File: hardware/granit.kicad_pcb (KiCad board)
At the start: 4 copper layers, 92 x 100 mm, 4 parts

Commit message: Draft component placement
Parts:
- added BT1: Battery_Cell, Battery:BatteryHolder_Keystone_3034_1x20mm, F.Cu at (32.0, 37.0)
- added C1: 10u, Capacitor_SMD:C_0805_2012Metric, F.Cu at (57.0, 104.5)
- added C10: 100u, Capacitor_Tantalum_SMD:CP_EIA-7343-31_Kemet-D, F.Cu at (55.0, 114.5)
- added C11: 100n, Capacitor_SMD:C_0805_2012Metric, F.Cu at (78.0, 115.5)
- added C12: 1n, Capacitor_SMD:C_0805_2012Metric, F.Cu at (65.0, 111.0)
- added C13: 10u, Capacitor_SMD:C_0805_2012Metric, F.Cu at (81.5, 111.0)
- added C14: 10u, Capacitor_SMD:C_0805_2012Metric, F.Cu at (87.5, 114.5)
- added C15: 10u, Capacitor_SMD:C_0805_2012Metric, F.Cu at (85.5, 114.5)
- added C16: 10u, Capacitor_SMD:C_0805_2012Metric, F.Cu at (83.5, 114.5)
- added C17: 10u, Capacitor_SMD:C_0805_2012Metric, F.Cu at (85.5, 111.0)
- added C18: 10u, Capacitor_SMD:C_0805_2012Metric, F.Cu at (83.5, 111.0)
- added C19: 100n, Capacitor_SMD:C_0805_2012Metric, F.Cu at (78.0, 107.5)
- added C2: 10u, Capacitor_SMD:C_0805_2012Metric, F.Cu at (54.0, 96.5)
- added C20: 1n, Capacitor_SMD:C_0805_2012Metric, F.Cu at (69.0, 110.0)
- added C21: 1.2n, Capacitor_SMD:C_0805_2012Metric, F.Cu at (70.0, 107.0)
- added C22: 100n, Capacitor_SMD:C_0805_2012Metric, F.Cu at (95.5, 80.0)
- added C23: 100n, Capacitor_SMD:C_0805_2012Metric, F.Cu at (39.0, 52.5)
- added C24: 100n, Capacitor_SMD:C_0805_2012Metric, F.Cu at (41.5, 52.5)
- added C25: 100n, Capacitor_SMD:C_0805_2012Metric, F.Cu at (36.5, 52.5)
- added C26: 15p, Capacitor_SMD:C_0805_2012Metric, F.Cu at (41.5, 73.0)
- added C27: 15p, Capacitor_SMD:C_0805_2012Metric, F.Cu at (39.5, 73.0)
- added C28: 100n, Capacitor_SMD:C_0805_2012Metric, F.Cu at (29.5, 68.0)
- added C29: 100n, Capacitor_SMD:C_0805_2012Metric, F.Cu at (32.0, 52.0)
- added C3: 10u, Capacitor_SMD:C_0805_2012Metric, F.Cu at (95.0, 109.5)
- added C30: 100n, Capacitor_SMD:C_0805_2012Metric, F.Cu at (37.5, 58.5)
- added C31: 100n, Capacitor_SMD:C_0805_2012Metric, F.Cu at (39.5, 58.5)
- added C32: 100n, Capacitor_SMD:C_0805_2012Metric, F.Cu at (35.5, 73.5)
- added C33: 100n, Capacitor_SMD:C_0805_2012Metric, F.Cu at (30.0, 62.0)
- added C34: 100n, Capacitor_SMD:C_0805_2012Metric, F.Cu at (103.5, 35.0)
- added C35: 100n, Capacitor_SMD:C_0805_2012Metric, F.Cu at (100.0, 30.0)
- added C36: 100n, Capacitor_SMD:C_0805_2012Metric, F.Cu at (100.0, 48.5)
- added C37: 100n, Capacitor_SMD:C_0805_2012Metric, F.Cu at (48.1, 34.6)
- added C38: 100n, Capacitor_SMD:C_0805_2012Metric, F.Cu at (109.0, 58.0)
- added C39: 100n, Capacitor_SMD:C_0805_2012Metric, F.Cu at (52.1, 34.3)
- added C4: 10u, Capacitor_SMD:C_0805_2012Metric, F.Cu at (94.5, 117.5)
- added C5: 10u, Capacitor_SMD:C_0805_2012Metric, F.Cu at (81.5, 114.5)
- added C6: 10u, Capacitor_SMD:C_0805_2012Metric, F.Cu at (63.0, 111.0)
- added C7: 10u, Capacitor_SMD:C_0805_2012Metric, F.Cu at (61.0, 111.0)
- added C8: 10u, Capacitor_SMD:C_0805_2012Metric, F.Cu at (63.0, 114.5)
- added C9: 10u, Capacitor_SMD:C_0805_2012Metric, F.Cu at (61.0, 114.5)
- added CM1: CM4, granit:Raspberry-Pi-4-Compute-Module, F.Cu at (85.5, 42.0)
- added D1: SK6812MINI-E, LED_SMD:LED_SK6812MINI-E_3.2x2.8mm_P1.5mm_ReverseMount, F.Cu at (109.0, 32.0)
- added D2: LED R, LED_SMD:LED_0805_2012Metric, F.Cu at (91.5, 35.5)
- added D3: LED G, LED_SMD:LED_0805_2012Metric, F.Cu at (91.5, 31.1)
- added F1: Fuse, Fuse:Fuse_2512_6332Metric, F.Cu at (99.5, 112.5)
- added IC1: ASM1061, granit:QFN50P700X700X90-49N-D, F.Cu at (35.5, 65.5)
- added J1: 12V Barrel, granit:BarrelJack_Wuerth_6941xx301002, F.Cu at (97.4, 102.8)
- added J2: 12V Screw Terminal, TerminalBlock_Phoenix:TerminalBlock_Phoenix_MKDS-1,5-2_1x02_P5.00mm_Horizontal, F.Cu at (107.1, 104.8)
- added J3: RJ45_RB1-125B8G1A, Connector_RJ:RJ45_UDE_RB1-125B8G1A, F.Cu at (93.8, 75.8)
- added J6: Conn_01x02, Connector_PinHeader_2.54mm:PinHeader_1x02_P2.54mm_Vertical, F.Cu at (78.3, 29.5)
- added J7: USB_C_Receptacle_USB2.0_14P, Connector_USB:USB_C_Receptacle_GCT_USB4105-xx-A_16P_TopMnt_Horizontal, F.Cu at (108.5, 51.5)
- added J8: Conn_01x03, Connector_PinHeader_2.54mm:PinHeader_1x03_P2.54mm_Vertical, F.Cu at (82.0, 29.5)
- added J9: SATA_22pin, Connector_SATA_SAS:SATA_Amphenol_10029364-001LF_Horizontal, F.Cu at (23.0, 79.5)
- added JP1: 12V_bridge, Jumper:SolderJumper-2_P1.3mm_Open_Pad1.0x1.5mm, F.Cu at (29.0, 105.5)
- added JP2: 5V_bridge, Jumper:SolderJumper-2_P1.3mm_Open_Pad1.0x1.5mm, F.Cu at (39.5, 116.5)
- added JP3: 3V3_bridge, Jumper:SolderJumper-2_P1.3mm_Open_Pad1.0x1.5mm, F.Cu at (47.0, 97.0)
- added JP4: USB_OTG, Jumper:SolderJumper-2_P1.3mm_Bridged_Pad1.0x1.5mm, F.Cu at (44.5, 83.5)
- added L1: SRN6045TA-3R3Y, Inductor_SMD:L_Bourns_SRN6045TA, F.Cu at (67.5, 116.1)
- added Q1: FDS4435BZ, granit:SO08-E3, F.Cu at (93.5, 113.6)
- added Q2: FDS4435BZ, granit:SO08-E3, F.Cu at (33.5, 106.0)
- added Q3: FDS4435BZ, granit:SO08-E3, F.Cu at (41.0, 112.0)
- added Q4: 2N7002, Package_TO_SOT_SMD:SOT-23, F.Cu at (71.5, 35.6)
- added R1: 10R, Resistor_SMD:R_0805_2012Metric, F.Cu at (74.5, 115.5)
- added R10: 12K, Resistor_SMD:R_0805_2012Metric, F.Cu at (34.0, 58.5)
- added R11: 750R, Resistor_SMD:R_0805_2012Metric, F.Cu at (27.5, 65.5)
- added R12: 100K, Resistor_SMD:R_0805_2012Metric, F.Cu at (32.0, 111.5)
- added R13: 100K, Resistor_SMD:R_0805_2012Metric, F.Cu at (46.0, 113.0)
- added R14: 10K, Resistor_SMD:R_0805_2012Metric, F.Cu at (35.0, 112.0)
- added R15: 10K, Resistor_SMD:R_0805_2012Metric, F.Cu at (47.0, 110.0)
- added R16: 10K, Resistor_SMD:R_0805_2012Metric, F.Cu at (101.5, 41.0)
- added R17: 330R, Resistor_SMD:R_0805_2012Metric, F.Cu at (96.0, 32.5)
- added R18: 330R, Resistor_SMD:R_0805_2012Metric, F.Cu at (96.0, 35.5)
- added R19: 330R, Resistor_SMD:R_0805_2012Metric, F.Cu at (102.0, 27.5)
- added R2: 12K, Resistor_SMD:R_0805_2012Metric, F.Cu at (67.0, 111.0)
- added R20: 5K1, Resistor_SMD:R_0805_2012Metric, F.Cu at (102.0, 48.5)
- added R21: 5K1, Resistor_SMD:R_0805_2012Metric, F.Cu at (102.5, 56.0)
- added R22: 4K7, Resistor_SMD:R_0805_2012Metric, F.Cu at (53.5, 24.6)
- added R23: 4K7, Resistor_SMD:R_0805_2012Metric, F.Cu at (53.0, 28.6)
- added R24: 10K, Resistor_SMD:R_0805_2012Metric, F.Cu at (57.0, 32.6)
- added R25: 10K, Resistor_SMD:R_0805_2012Metric, F.Cu at (61.0, 32.1)
- added R26: 10K, Resistor_SMD:R_0805_2012Metric, F.Cu at (61.0, 36.6)
- added R27: 10K, Resistor_SMD:R_0805_2012Metric, F.Cu at (65.5, 35.6)
- added R3: 20K, Resistor_SMD:R_0805_2012Metric, F.Cu at (71.0, 110.0)
- added R4: 2K2, Resistor_SMD:R_0805_2012Metric, F.Cu at (64.0, 108.1)
- added R5: 330R, Resistor_SMD:R_0805_2012Metric, F.Cu at (108.0, 60.5)
- added R6: 330R, Resistor_SMD:R_0805_2012Metric, F.Cu at (105.5, 79.5)
- added R7: 10R, Resistor_SMD:R_0805_2012Metric, F.Cu at (92.0, 80.0)
- added R8: 10K, Resistor_SMD:R_0805_2012Metric, F.Cu at (93.5, 41.0)
- added R9: 750R, Resistor_SMD:R_0805_2012Metric, F.Cu at (42.5, 64.0)
- added SW1: SW_Push, Button_Switch_SMD:SW_Push_1TS009xxxx-xxxx-xxxx_6x6x5mm, F.Cu at (107.5, 40.5)
- added TP1: TestPoint, TestPoint:TestPoint_Pad_2.0x2.0mm, F.Cu at (58.0, 110.5)
- added TP2: TestPoint, TestPoint:TestPoint_Pad_2.0x2.0mm, F.Cu at (88.0, 111.0)
- added TP3: TestPoint, TestPoint:TestPoint_Pad_2.0x2.0mm, F.Cu at (110.0, 109.5)
- added U1: NCP1117-3.3_SOT223, Package_TO_SOT_SMD:SOT-223-3_TabPin2, F.Cu at (52.0, 102.0)
- added U2: AP64501SP-13, granit:SOIC-8-1EP_3.9x4.9mm_P1.27mm_EP2.95x4.9mm_Mask2.71x3.4mm_ThermalVias, F.Cu at (76.0, 111.6)
- added U3: 74AHCT1G125, Package_TO_SOT_SMD:SOT-23-5, F.Cu at (103.5, 31.0)
- added U4: DS3231MZ, Package_SO:SOIC-8_3.9x4.9mm_P1.27mm, F.Cu at (67.2, 28.8)
- added U5: USBLC6-2SC6, Package_TO_SOT_SMD:SOT-23-6, F.Cu at (101.0, 52.0)
- added U6: 74AHCT1G32, Package_TO_SOT_SMD:SOT-23-5, F.Cu at (59.5, 26.6)
- added Y1: Crystal, Crystal:Crystal_SMD_3215-2Pin_3.2x1.5mm, F.Cu at (40.5, 70.0)
- moved H4 0.82 mm to (107.9, 115.2)

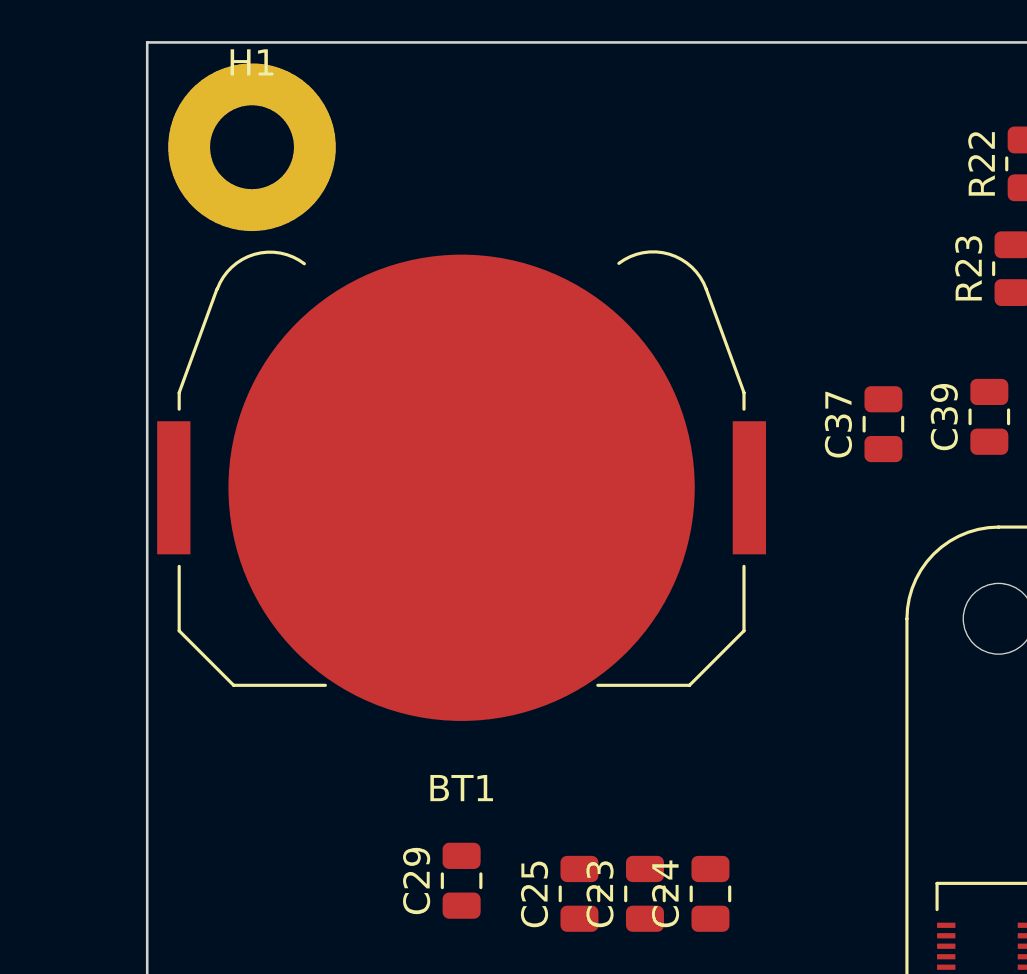
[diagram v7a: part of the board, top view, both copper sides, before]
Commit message: Use lightweight CM4 3D model from pedalboard-hw (7MB vs 64MB)
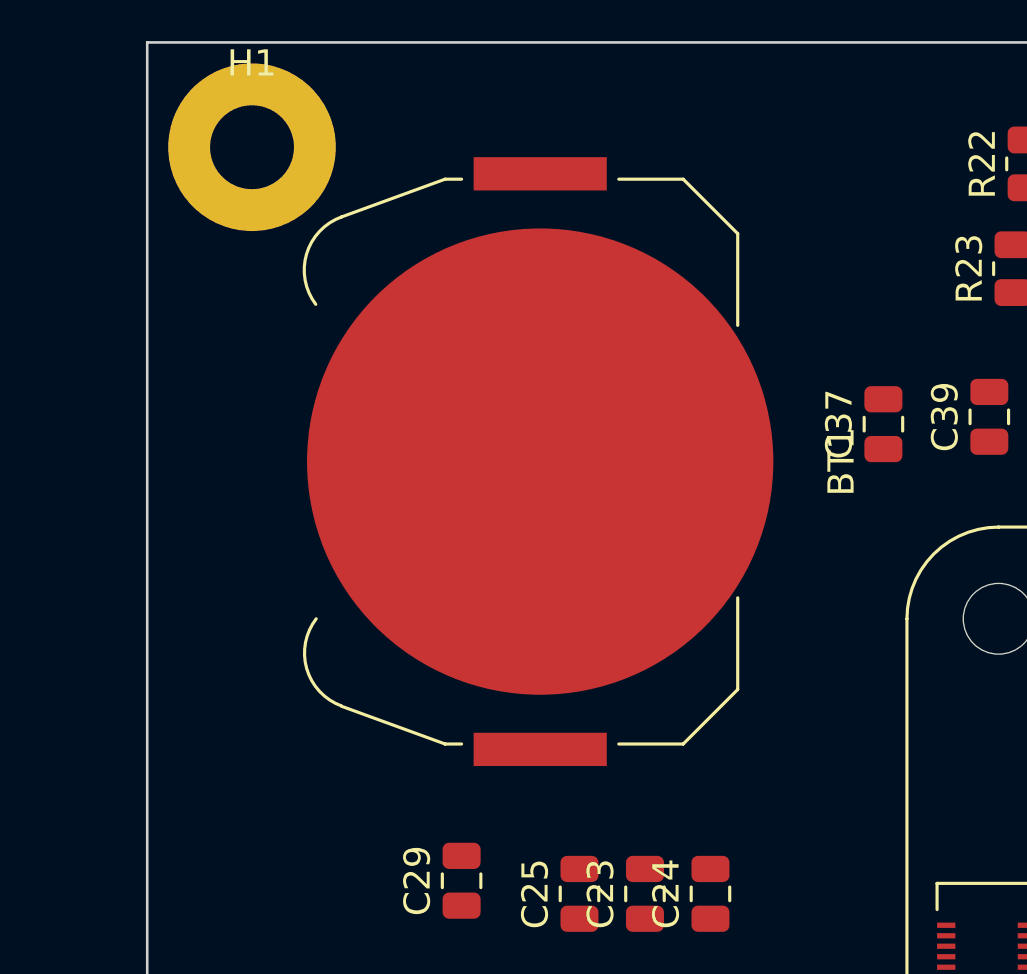
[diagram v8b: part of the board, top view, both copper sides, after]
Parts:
- moved BT1 3.16 mm to (35.0, 36.0), turned to -90 degrees
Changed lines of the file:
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@@
 	)
 	(footprint "MountingHole:MountingHole_3.2mm_M3_Pad_Via"
+		(locked yes)
 		(layer "F.Cu")
 		(at 24 24)
@@
 	(footprint "Battery:BatteryHolder_Keystone_3034_1x20mm"
 		(layer "F.Cu")
-		(at 32 37 180)
+		(at 35 36 -90)
 		(descr "Keystone 3034 SMD battery holder for 2020, 2025 and 2032 coincell batteries. http://www.keyelco.com/product-pdf.cfm?p=798")
 		(tags "Keystone type 3034 coin cell retainer")
 		(property "Reference" "BT1"
-			(at 0 -11.5 0)
+			(at 0 -11.5 90)
 			(layer "F.SilkS")
 			(effects
@@
 		)
 		(property "Value" "Battery_Cell"
-			(at 0 11.5 0)
+			(at 0 11.5 90)
 			(layer "F.Fab")
 			(effects
@@
 		)
 		(property "Datasheet" ""
-			(at 0 0 180)
+			(at 0 0 270)
 			(unlocked yes)
 			(layer "F.Fab")
@@
 		)
 		(property "Description" "Single-cell battery"
-			(at 0 0 180)
+			(at 0 0 270)
 			(unlocked yes)
 			(layer "F.Fab")
@@
 		)
 		(property "Sim.Device" "V"
-			(at 0 0 180)
+			(at 0 0 270)
 			(unlocked yes)
 			(layer "F.Fab")
@@
 		)
 		(property "Sim.Type" "DC"
-			(at 0 0 180)
+			(at 0 0 270)
 			(unlocked yes)
 			(layer "F.Fab")
@@
 		)
 		(property "Sim.Pins" "1=+ 2=-"
-			(at 0 0 180)
+			(at 0 0 270)
 			(unlocked yes)
 			(layer "F.Fab")
@@
 		(duplicate_pad_numbers_are_jumpers no)
 		(fp_line
-			(start 10.78 3.63)
-			(end 9.34 7.58)
+			(start -10.78 3.63)
+			(end -9.34 7.58)
 			(stroke
 				(width 0.12)
@@
 		)
 		(fp_line
-			(start 10.78 3)
-			(end 10.78 3.63)
+			(start 10.78 3.63)
+			(end 9.34 7.58)
 			(stroke
 				(width 0.12)
@@
 		)
 		(fp_line
-			(start 10.78 -5.46)
-			(end 10.78 -3)
+			(start -10.78 3)
+			(end -10.78 3.63)
 			(stroke
 				(width 0.12)
@@
 		)
 		(fp_line
-			(start 8.7 -7.54)
-			(end 10.78 -5.46)
+			(start 10.78 3)
+			(end 10.78 3.63)
 			(stroke
 				(width 0.12)
@@
 		)
 		(fp_line
-			(start 8.7 -7.54)
-			(end 5.2 -7.54)
+			(start -10.78 -5.46)
+			(end -10.78 -3)
 			(stroke
 				(width 0.12)
@@
 		)
 		(fp_line
-			(start -5.2 -7.54)
-			(end -8.7 -7.54)
+			(start 10.78 -5.46)
+			(end 10.78 -3)
 			(stroke
 				(width 0.12)
@@
 		)
 		(fp_line
-			(start -10.78 3.63)
-			(end -9.34 7.58)
+			(start -5.2 -7.54)
+			(end -8.7 -7.54)
 			(stroke
 				(width 0.12)
@@
 		)
 		(fp_line
-			(start -10.78 3)
-			(end -10.78 3.63)
+			(start 8.7 -7.54)
+			(end 10.78 -5.46)
 			(stroke
 				(width 0.12)
@@
 		)
 		(fp_line
-			(start -10.78 -5.46)
-			(end -10.78 -3)
+			(start 8.7 -7.54)
+			(end 5.2 -7.54)
 			(stroke
 				(width 0.12)
@@
 		)
 		(fp_arc
-			(start 9.325243 7.588169)
-			(mid 7.90634 8.911668)
-			(end 6 8.55)
+			(start -6.003354 8.56653)
+			(mid -7.921654 8.918738)
+			(end -9.34 7.58)
 			(stroke
 				(width 0.12)
@@
 		)
 		(fp_arc
-			(start -6.003354 8.56653)
-			(mid -7.921654 8.918738)
-			(end -9.34 7.58)
+			(start 9.325243 7.588169)
+			(mid 7.90634 8.911668)
+			(end 6 8.55)
 			(stroke
 				(width 0.12)
@@
 		)
 		(fp_line
-			(start 11.87 2.79)
-			(end 11.87 -2.79)
+			(start 9.43 7.63)
+			(end 10.88 3.64)
 			(stroke
 				(width 0.05)
@@
 		)
 		(fp_line
-			(start 11.87 -2.79)
-			(end 10.88 -2.79)
+			(start -10.88 3.64)
+			(end -9.44 7.62)
 			(stroke
 				(width 0.05)
@@
 		)
 		(fp_line
-			(start 10.88 2.79)
-			(end 11.87 2.79)
+			(start -11.87 2.79)
+			(end -10.88 2.79)
 			(stroke
 				(width 0.05)
@@
 		)
 		(fp_line
-			(start 10.88 -2.79)
-			(end 10.88 -5.5)
+			(start -10.88 2.79)
+			(end -10.88 3.64)
 			(stroke
 				(width 0.05)
@@
 		)
 		(fp_line
-			(start 10.88 -5.5)
-			(end 8.74 -7.64)
+			(start 10.88 2.79)
+			(end 11.87 2.79)
 			(stroke
 				(width 0.05)
@@
 		)
 		(fp_line
-			(start 9.43 7.63)
-			(end 10.88 3.64)
+			(start 11.87 2.79)
+			(end 11.87 -2.79)
 			(stroke
 				(width 0.05)
@@
 		)
 		(fp_line
-			(start 8.74 -7.64)
-			(end 7.2 -7.64)
+			(start -11.87 -2.79)
+			(end -11.87 2.79)
 			(stroke
 				(width 0.05)
@@
 		)
 		(fp_line
-			(start -7.2 -7.64)
-			(end -8.74 -7.64)
+			(start -10.88 -2.79)
+			(end -11.87 -2.79)
 			(stroke
 				(width 0.05)
@@
 		)
 		(fp_line
-			(start -8.74 -7.64)
-			(end -10.88 -5.5)
+			(start 10.88 -2.79)
+			(end 10.88 -5.5)
 			(stroke
 				(width 0.05)
@@
 		)
 		(fp_line
-			(start -10.88 3.64)
-			(end -9.44 7.62)
+			(start 11.87 -2.79)
+			(end 10.88 -2.79)
 			(stroke
 				(width 0.05)
@@
 		)
 		(fp_line
-			(start -10.88 2.79)
-			(end -10.88 3.64)
+			(start -10.88 -5.5)
+			(end -10.88 -2.79)
 			(stroke
 				(width 0.05)
@@
 		)
 		(fp_line
-			(start -10.88 -2.79)
-			(end -11.87 -2.79)
+			(start 10.88 -5.5)
+			(end 8.74 -7.64)
 			(stroke
 				(width 0.05)
@@
 		)
 		(fp_line
-			(start -10.88 -5.5)
-			(end -10.88 -2.79)
+			(start -8.74 -7.64)
+			(end -10.88 -5.5)
 			(stroke
 				(width 0.05)
@@
 		)
 		(fp_line
-			(start -11.87 2.79)
-			(end -10.88 2.79)
+			(start -7.2 -7.64)
+			(end -8.74 -7.64)
 			(stroke
 				(width 0.05)
@@
 		)
 		(fp_line
-			(start -11.87 -2.79)
-			(end -11.87 2.79)
+			(start 8.74 -7.64)
+			(end 7.2 -7.64)
 			(stroke
 				(width 0.05)
@@
 		)
 		(fp_arc
-			(start 9.415144 7.621341)
-			(mid 7.944017 9.000493)
-			(end 5.96 8.64)
+			(start -5.956965 8.654604)
+			(mid -7.953941 9.011629)
+			(end -9.43 7.62)
 			(stroke
 				(width 0.05)
@@
 		)
 		(fp_arc
-			(start -5.956965 8.654604)
-			(mid -7.953941 9.011629)
-			(end -9.43 7.62)
+			(start 9.415144 7.621341)
+			(mid 7.944017 9.000493)
+			(end 5.96 8.64)
 			(stroke
 				(width 0.05)
@@
 		)
 		(fp_line
-			(start 10.63 3.6)
-			(end 9.19 7.53)
+			(start -9.19 7.53)
+			(end -10.63 3.6)
 			(stroke
 				(width 0.1)
@@
 		)
 		(fp_line
-			(start 10.63 -5.4)
-			(end 10.63 3.6)
+			(start -10.63 3.6)
+			(end -10.63 -5.4)
 			(stroke
 				(width 0.1)
@@
 		)
 		(fp_line
-			(start 8.64 -7.39)
-			(end 10.63 -5.4)
+			(start 10.63 3.6)
+			(end 9.19 7.53)
 			(stroke
 				(width 0.1)
@@
 		)
 		(fp_line
-			(start -8.64 -7.39)
-			(end 8.64 -7.39)
+			(start -10.63 -5.4)
+			(end -8.64 -7.39)
 			(stroke
 				(width 0.1)
@@
 		)
 		(fp_line
-			(start -9.19 7.53)
-			(end -10.63 3.6)
+			(start 10.63 -5.4)
+			(end 10.63 3.6)
 			(stroke
 				(width 0.1)
@@
 		)
 		(fp_line
-			(start -10.63 3.6)
-			(end -10.63 -5.4)
+			(start -8.64 -7.39)
+			(end 8.64 -7.39)
 			(stroke
 				(width 0.1)
@@
 		)
 		(fp_line
-			(start -10.63 -5.4)
-			(end -8.64 -7.39)
+			(start 8.64 -7.39)
+			(end 10.63 -5.4)
 			(stroke
 				(width 0.1)
@@
 		)
 		(fp_arc
-			(start 9.180727 7.528882)
-			(mid 7.868698 8.760067)
-			(end 6.1 8.43)
+			(start -6.096146 8.438508)
+			(mid -7.87328 8.768206)
+			(end -9.19 7.53)
 			(stroke
 				(width 0.1)
@@
 		)
 		(fp_arc
-			(start -6.096146 8.438508)
-			(mid -7.87328 8.768206)
-			(end -9.19 7.53)
+			(start 9.180727 7.528882)
+			(mid 7.868698 8.760067)
+			(end 6.1 8.43)
 			(stroke
 				(width 0.1)
@@
 		)
 		(fp_text user "${REFERENCE}"
-			(at 0 -2.9 0)
+			(at 0 -2.9 90)
 			(layer "F.Fab")
 			(effects
@@
 		)
 		(pad "1" smd rect
-			(at -10.985 0 180)
+			(at -10.985 0 270)
 			(size 1.27 5.08)
 			(layers "F.Cu" "F.Mask" "F.Paste")
@@
 		)
 		(pad "1" smd rect
-			(at 10.985 0 180)
+			(at 10.985 0 270)
 			(size 1.27 5.08)
 			(layers "F.Cu" "F.Mask" "F.Paste")
@@
 		)
 		(pad "2" smd circle
-			(at 0 0 180)
+			(at 0 0 270)
 			(size 17.8 17.8)
 			(layers "F.Cu" "F.Mask")
@@
 	)
 	(footprint "MountingHole:MountingHole_3.2mm_M3_Pad_Via"
+		(locked yes)
 		(layer "F.Cu")
 		(at 24 116)
@@
 	)
 	(footprint "MountingHole:MountingHole_3.2mm_M3_Pad_Via"
+		(locked yes)
 		(layer "F.Cu")
 		(at 107.859281 115.19664)
@@
 	)
 	(footprint "MountingHole:MountingHole_3.2mm_M3_Pad_Via"
+		(locked yes)
 		(layer "F.Cu")
 		(at 108 24)
